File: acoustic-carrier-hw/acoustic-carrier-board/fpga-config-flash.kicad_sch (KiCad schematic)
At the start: 20 parts, among them IC1 ECP5-BGA256, J16 Conn_01x08_Socket, J6 Conn_01x10_Socket, U4 W25Q128JVS, U9 W25Q128JVS

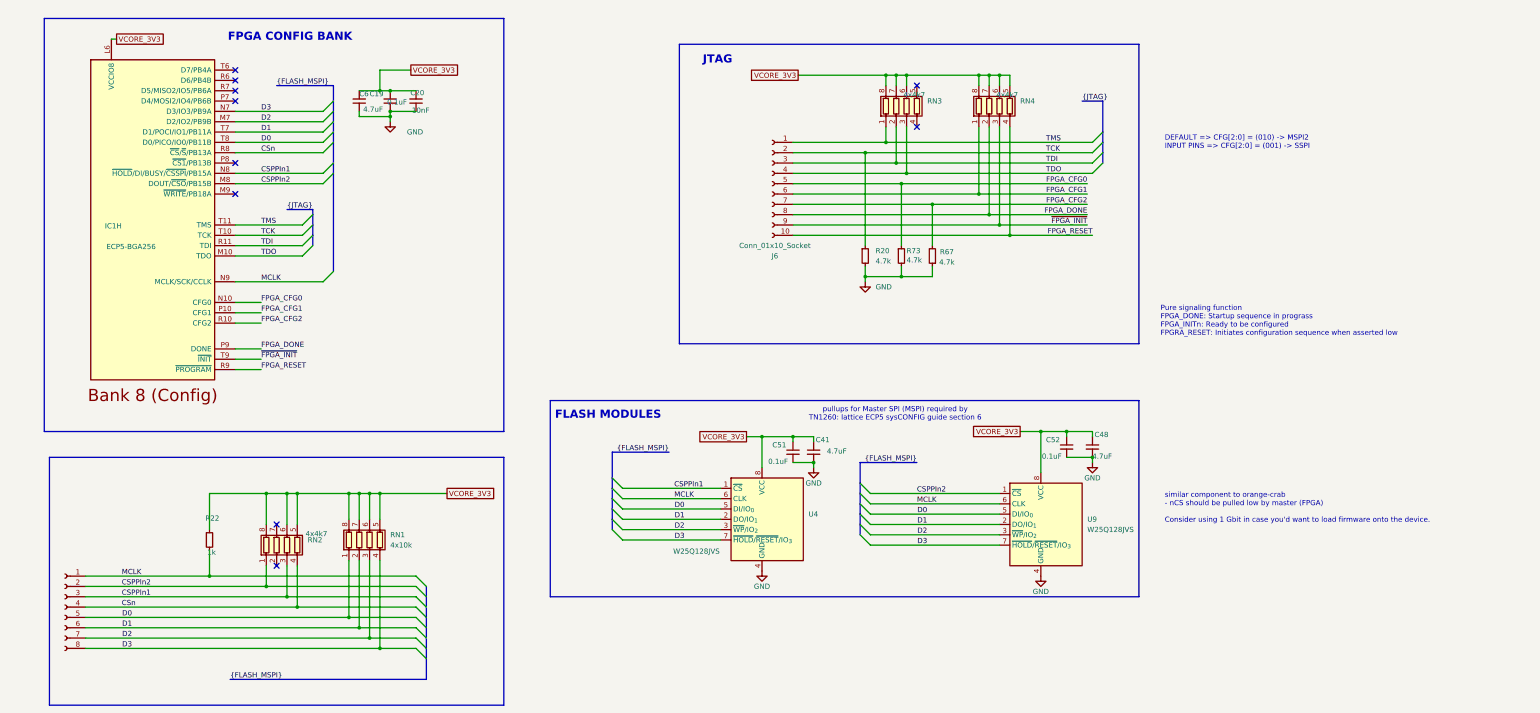
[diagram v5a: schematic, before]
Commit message: [carrier] Added testpoints
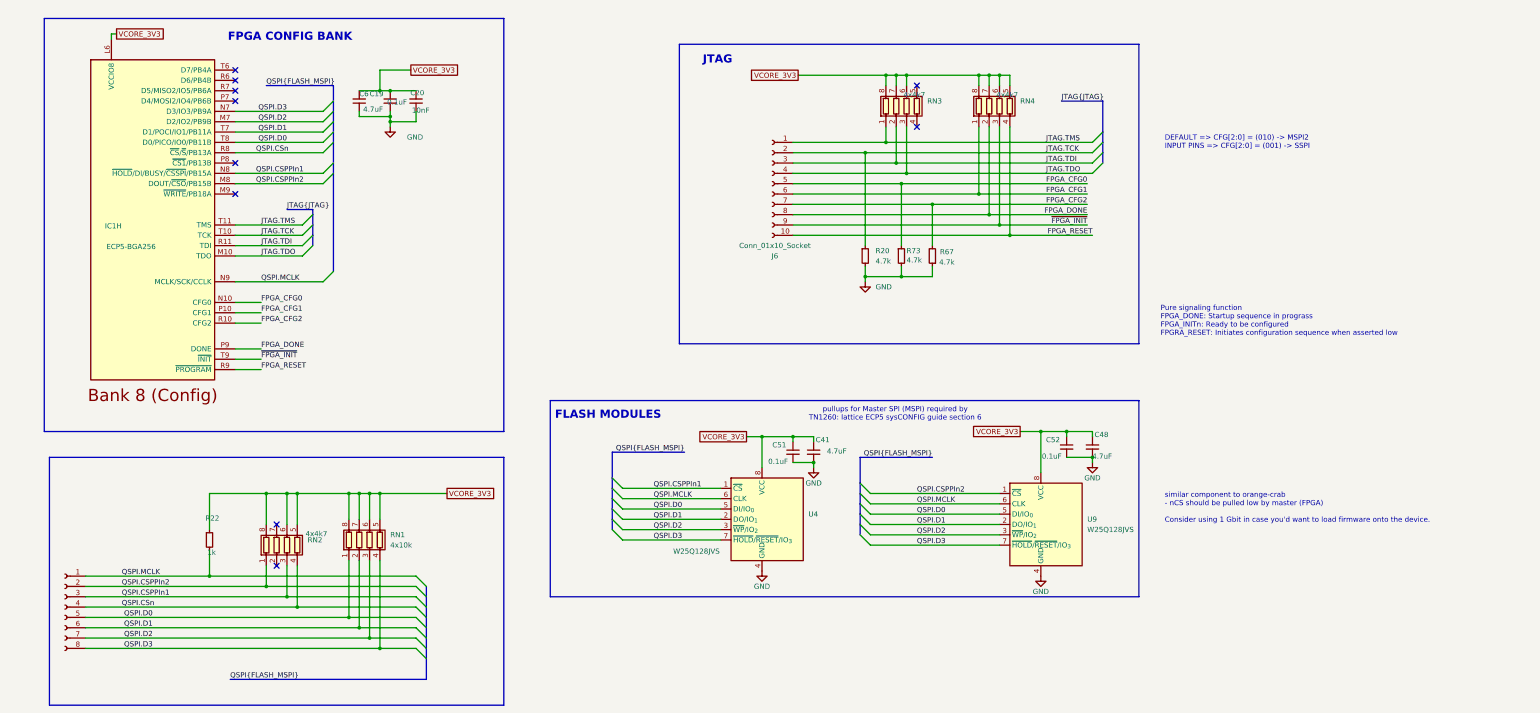
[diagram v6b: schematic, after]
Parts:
- C20: LPN CL05B103KB5NNNC -> C15195; MPN C15195 -> CL05B103KB5NNNC
- R20, R67, R73: LPN 0402WGF4701TCE -> C25900; MPN C25900 -> 0402WGF4701TCE
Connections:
- net CSPPIn1 renamed QSPI.CSPPIn1
- net CSPPIn2 renamed QSPI.CSPPIn2
- net CSn renamed QSPI.CSn
- net D0 renamed QSPI.D0
- net D1 renamed QSPI.D1
- net D2 renamed QSPI.D2
- net D3 renamed QSPI.D3
- net MCLK renamed QSPI.MCLK
- net TCK renamed JTAG.TCK
- net TDI renamed JTAG.TDI
- net TDO renamed JTAG.TDO
- net TMS renamed JTAG.TMS

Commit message: [carrier] Finished rough layout, p (put together according to component category
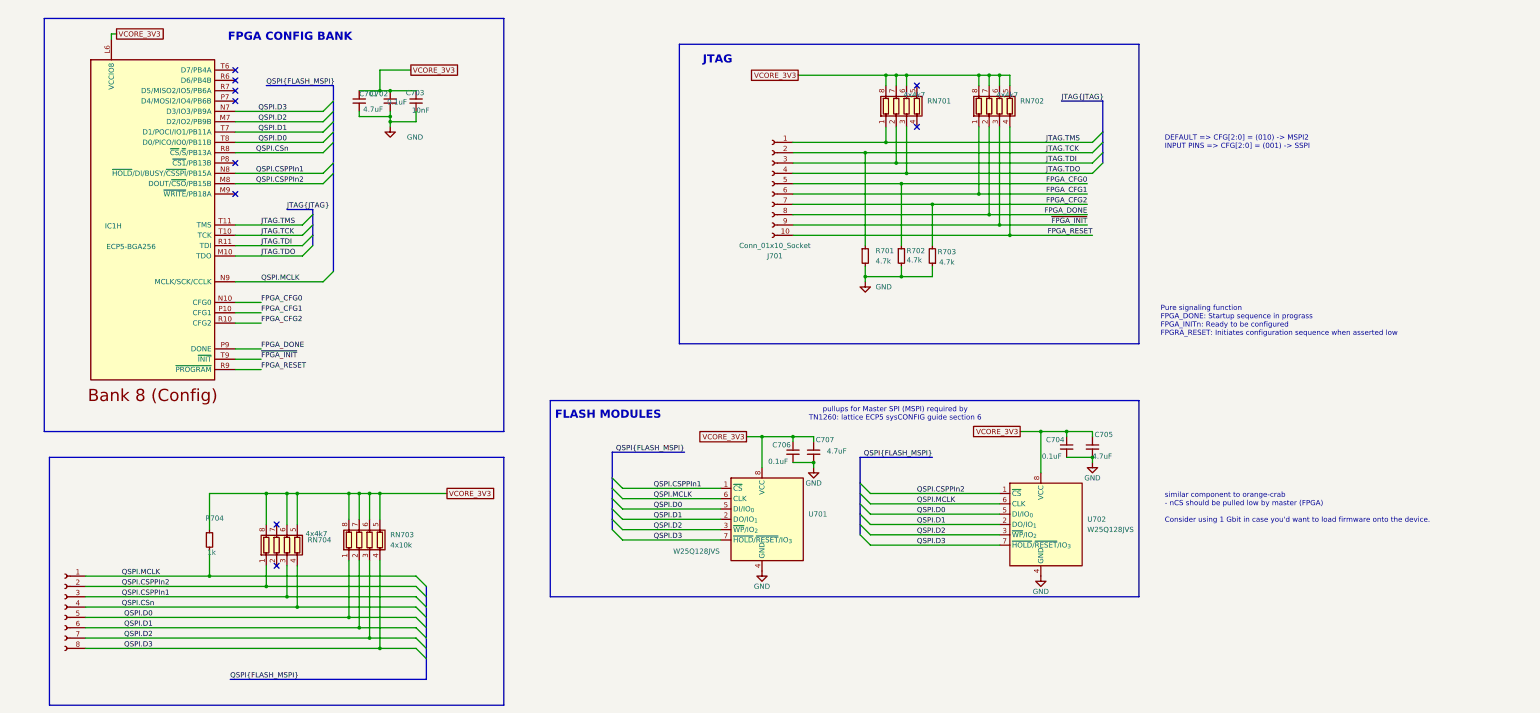
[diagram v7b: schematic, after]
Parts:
- renumbered C6 to C701, C19 to C702, C20 to C703, C52 to C704, C48 to C705, C51 to C706, C41 to C707, J6 to J701, J16 to J702, R20 to R701, R73 to R702, R67 to R703, R22 to R704, RN3 to RN701, RN4 to RN702, RN1 to RN703, RN2 to RN704, U4 to U701, U9 to U702
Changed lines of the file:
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@@
 		(on_board yes)
 		(dnp no)
-		(property "Reference" "#PWR051"
+		(property "Reference" "#PWR0703"
 			(at 271.78 132.08 0)
 			(effects
@@
 			(project "acoustic-carrier-board"
 				(path "/25b015c9-ab13-4427-b72c-b6f348597100/36da1f88-b4f8-4b81-86e1-fac0fb6202fa"
-					(reference "#PWR051")
+					(reference "#PWR0703")
 					(unit 1)
 				)
@@
 		(on_board yes)
 		(dnp no)
-		(property "Reference" "C20"
+		(property "Reference" "C703"
 			(at 107.442 34.798 0)
 			(effects
@@
 			(project "acoustic-carrier-board"
 				(path "/25b015c9-ab13-4427-b72c-b6f348597100/36da1f88-b4f8-4b81-86e1-fac0fb6202fa"
-					(reference "C20")
+					(reference "C703")
 					(unit 1)
 				)
@@
 		(on_board yes)
 		(dnp no)
-		(property "Reference" "C51"
+		(property "Reference" "C706"
 			(at 193.04 121.412 0)
 			(effects
@@
 			(project "acoustic-carrier-board"
 				(path "/25b015c9-ab13-4427-b72c-b6f348597100/36da1f88-b4f8-4b81-86e1-fac0fb6202fa"
-					(reference "C51")
+					(reference "C706")
 					(unit 1)
 				)
@@
 		(on_board yes)
 		(dnp no)
-		(property "Reference" "C6"
+		(property "Reference" "C701"
 			(at 91.44 35.052 0)
 			(effects
@@
 			(project "acoustic-carrier-board"
 				(path "/25b015c9-ab13-4427-b72c-b6f348597100/36da1f88-b4f8-4b81-86e1-fac0fb6202fa"
-					(reference "C6")
+					(reference "C701")
 					(unit 1)
 				)
@@
 		(on_board yes)
 		(dnp no)
-		(property "Reference" "J6"
+		(property "Reference" "J701"
 			(at 193.675 74.93 0)
 			(effects
@@
 			(project "acoustic-carrier-board"
 				(path "/25b015c9-ab13-4427-b72c-b6f348597100/36da1f88-b4f8-4b81-86e1-fac0fb6202fa"
-					(reference "J6")
+					(reference "J701")
 					(unit 1)
 				)
@@
 		(on_board yes)
 		(dnp no)
-		(property "Reference" "R67"
+		(property "Reference" "R703"
 			(at 235.966 73.914 0)
 			(effects
@@
 			(project "acoustic-carrier-board"
 				(path "/25b015c9-ab13-4427-b72c-b6f348597100/36da1f88-b4f8-4b81-86e1-fac0fb6202fa"
-					(reference "R67")
+					(reference "R703")
 					(unit 1)
 				)
@@
 		(on_board yes)
 		(dnp no)
-		(property "Reference" "C41"
+		(property "Reference" "C707"
 			(at 203.708 120.142 0)
 			(effects
@@
 			(project "acoustic-carrier-board"
 				(path "/25b015c9-ab13-4427-b72c-b6f348597100/36da1f88-b4f8-4b81-86e1-fac0fb6202fa"
-					(reference "C41")
+					(reference "C707")
 					(unit 1)
 				)
@@
 		(on_board yes)
 		(dnp no)
-		(property "Reference" "#PWR047"
+		(property "Reference" "#PWR0704"
 			(at 203.2 133.35 0)
 			(effects
@@
 			(project "acoustic-carrier-board"
 				(path "/25b015c9-ab13-4427-b72c-b6f348597100/36da1f88-b4f8-4b81-86e1-fac0fb6202fa"
-					(reference "#PWR047")
+					(reference "#PWR0704")
 					(unit 1)
 				)
@@
 		(on_board yes)
 		(dnp no)
-		(property "Reference" "C48"
+		(property "Reference" "C705"
 			(at 272.288 118.872 0)
 			(effects
@@
 			(project "acoustic-carrier-board"
 				(path "/25b015c9-ab13-4427-b72c-b6f348597100/36da1f88-b4f8-4b81-86e1-fac0fb6202fa"
-					(reference "C48")
+					(reference "C705")
 					(unit 1)
 				)
@@
 		(on_board yes)
 		(dnp no)
-		(property "Reference" "R22"
+		(property "Reference" "R704"
 			(at 53.594 139.446 0)
 			(effects
@@
 			(project "acoustic-carrier-board"
 				(path "/25b015c9-ab13-4427-b72c-b6f348597100/36da1f88-b4f8-4b81-86e1-fac0fb6202fa"
-					(reference "R22")
+					(reference "R704")
 					(unit 1)
 				)
@@
 		(dnp no)
 		(fields_autoplaced yes)
-		(property "Reference" "U9"
+		(property "Reference" "U702"
 			(at 270.51 139.6999 0)
 			(effects
@@
 			(project "acoustic-carrier-board"
 				(path "/25b015c9-ab13-4427-b72c-b6f348597100/36da1f88-b4f8-4b81-86e1-fac0fb6202fa"
-					(reference "U9")
+					(reference "U702")
 					(unit 1)
 				)
@@
 		(dnp no)
 		(fields_autoplaced yes)
-		(property "Reference" "RN1"
+		(property "Reference" "RN703"
 			(at 99.06 143.5099 0)
 			(effects
@@
 			(project "acoustic-carrier-board"
 				(path "/25b015c9-ab13-4427-b72c-b6f348597100/36da1f88-b4f8-4b81-86e1-fac0fb6202fa"
-					(reference "RN1")
+					(reference "RN703")
 					(unit 1)
 				)
@@
 		(on_board yes)
 		(dnp no)
-		(property "Reference" "J16"
+		(property "Reference" "J702"
 			(at 19.685 176.53 0)
 			(effects
@@
 			(project "acoustic-carrier-board"
 				(path "/25b015c9-ab13-4427-b72c-b6f348597100/36da1f88-b4f8-4b81-86e1-fac0fb6202fa"
-					(reference "J16")
+					(reference "J702")
 					(unit 1)
 				)
@@
 		(on_board yes)
 		(dnp no)
-		(property "Reference" "#PWR043"
+		(property "Reference" "#PWR0706"
 			(at 259.08 160.02 0)
 			(effects
@@
 			(project "acoustic-carrier-board"
 				(path "/25b015c9-ab13-4427-b72c-b6f348597100/36da1f88-b4f8-4b81-86e1-fac0fb6202fa"
-					(reference "#PWR043")
+					(reference "#PWR0706")
 					(unit 1)
 				)
@@
 		(on_board yes)
 		(dnp no)
-		(property "Reference" "#PWR039"
+		(property "Reference" "#PWR0705"
 			(at 190.5 158.75 0)
 			(effects
@@
 			(project "acoustic-carrier-board"
 				(path "/25b015c9-ab13-4427-b72c-b6f348597100/36da1f88-b4f8-4b81-86e1-fac0fb6202fa"
-					(reference "#PWR039")
+					(reference "#PWR0705")
 					(unit 1)
 				)
@@
 		(dnp no)
 		(fields_autoplaced yes)
-		(property "Reference" "R20"
+		(property "Reference" "R701"
 			(at 218.44 73.6599 0)
 			(effects
@@
 			(project "acoustic-carrier-board"
 				(path "/25b015c9-ab13-4427-b72c-b6f348597100/36da1f88-b4f8-4b81-86e1-fac0fb6202fa"
-					(reference "R20")
+					(reference "R701")
 					(unit 1)
 				)
@@
 		(on_board yes)
 		(dnp no)
-		(property "Reference" "U4"
+		(property "Reference" "U701"
 			(at 201.93 138.4299 0)
 			(effects
@@
 			(project "acoustic-carrier-board"
 				(path "/25b015c9-ab13-4427-b72c-b6f348597100/36da1f88-b4f8-4b81-86e1-fac0fb6202fa"
-					(reference "U4")
+					(reference "U701")
 					(unit 1)
 				)
@@
 		(dnp no)
 		(fields_autoplaced yes)
-		(property "Reference" "#PWR036"
+		(property "Reference" "#PWR0702"
 			(at 215.9 87.63 0)
 			(effects
@@
 			(project "acoustic-carrier-board"
 				(path "/25b015c9-ab13-4427-b72c-b6f348597100/36da1f88-b4f8-4b81-86e1-fac0fb6202fa"
-					(reference "#PWR036")
+					(reference "#PWR0702")
 					(unit 1)
 				)
@@
 		(on_board yes)
 		(dnp no)
-		(property "Reference" "R73"
+		(property "Reference" "R702"
 			(at 226.06 73.66 0)
 			(effects
@@
 			(project "acoustic-carrier-board"
 				(path "/25b015c9-ab13-4427-b72c-b6f348597100/36da1f88-b4f8-4b81-86e1-fac0fb6202fa"
-					(reference "R73")
+					(reference "R702")
 					(unit 1)
 				)
@@
 		(on_board yes)
 		(dnp no)
-		(property "Reference" "#PWR032"
+		(property "Reference" "#PWR0701"
 			(at 99.06 49.53 0)
 			(effects
@@
 			(project "acoustic-carrier-board"
 				(path "/25b015c9-ab13-4427-b72c-b6f348597100/36da1f88-b4f8-4b81-86e1-fac0fb6202fa"
-					(reference "#PWR032")
+					(reference "#PWR0701")
 					(unit 1)
 				)
@@
 		(on_board yes)
 		(dnp no)
-		(property "Reference" "RN4"
+		(property "Reference" "RN702"
 			(at 254 36.8299 0)
 			(effects
@@
 			(project "acoustic-carrier-board"
 				(path "/25b015c9-ab13-4427-b72c-b6f348597100/36da1f88-b4f8-4b81-86e1-fac0fb6202fa"
-					(reference "RN4")
+					(reference "RN702")
 					(unit 1)
 				)
@@
 		(on_board yes)
 		(dnp no)
-		(property "Reference" "C19"
+		(property "Reference" "C702"
 			(at 93.98 35.052 0)
 			(effects
@@
 			(project "acoustic-carrier-board"
 				(path "/25b015c9-ab13-4427-b72c-b6f348597100/36da1f88-b4f8-4b81-86e1-fac0fb6202fa"
-					(reference "C19")
+					(reference "C702")
 					(unit 1)
 				)
@@
 		(on_board yes)
 		(dnp no)
-		(property "Reference" "RN2"
+		(property "Reference" "RN704"
 			(at 78.74 144.7799 0)
 			(effects
@@
 			(project "acoustic-carrier-board"
 				(path "/25b015c9-ab13-4427-b72c-b6f348597100/36da1f88-b4f8-4b81-86e1-fac0fb6202fa"
-					(reference "RN2")
+					(reference "RN704")
 					(unit 1)
 				)
@@
 		(on_board yes)
 		(dnp no)
-		(property "Reference" "RN3"
+		(property "Reference" "RN701"
 			(at 231.14 36.8299 0)
 			(effects
@@
 			(project "acoustic-carrier-board"
 				(path "/25b015c9-ab13-4427-b72c-b6f348597100/36da1f88-b4f8-4b81-86e1-fac0fb6202fa"
-					(reference "RN3")
+					(reference "RN701")
 					(unit 1)
 				)
@@
 		(on_board yes)
 		(dnp no)
-		(property "Reference" "C52"
+		(property "Reference" "C704"
 			(at 260.35 120.142 0)
 			(effects
@@
 			(project "acoustic-carrier-board"
 				(path "/25b015c9-ab13-4427-b72c-b6f348597100/36da1f88-b4f8-4b81-86e1-fac0fb6202fa"
-					(reference "C52")
+					(reference "C704")
 					(unit 1)
 				)

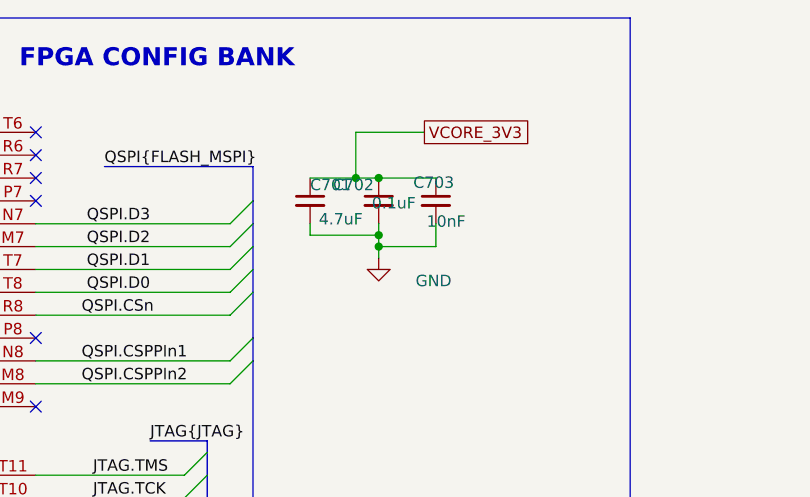
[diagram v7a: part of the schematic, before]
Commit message: [carrier] Removed USB-switch, placed decouplpling for DDR3 and ECP5U (next) consider adding buffers on CC1 and CC2 pins
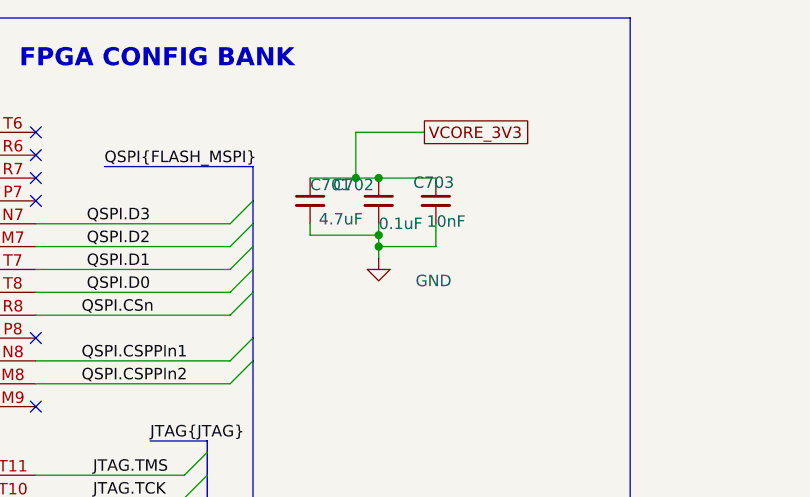
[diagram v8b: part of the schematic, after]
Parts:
- C702, C704, C706: footprint Capacitor_SMD:C_0402_1005Metric -> Capacitor_SMD:C_0201_0603Metric; LPN C307331 -> C22435929; MPN CL05B104KB54PNC -> CGA0201X7R104K160ET
- C703: footprint Capacitor_SMD:C_0402_1005Metric -> Capacitor_SMD:C_0201_0603Metric; LPN C15195 -> C285010; MPN CL05B103KB5NNNC -> 0201B103K250NT
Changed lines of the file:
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@@
 			)
 		)
-		(property "Footprint" "Capacitor_SMD:C_0402_1005Metric"
+		(property "Footprint" "Capacitor_SMD:C_0201_0603Metric"
 			(at 105.41 36.83 0)
 			(effects
@@
 			)
 		)
-		(property "Datasheet" "https://jlcpcb.com/api/file/downloadByFileSystemAccessId/8579707307011465216"
+		(property "Datasheet" "https://jlcpcb.com/api/file/downloadByFileSystemAccessId/8589040499521306624"
 			(at 105.41 36.83 0)
 			(effects
@@
 			)
 		)
-		(property "LPN" "C15195"
+		(property "LPN" "C285010"
 			(at 105.41 36.83 0)
 			(effects
@@
 			)
 		)
-		(property "MPN" "CL05B103KB5NNNC"
+		(property "MPN" "0201B103K250NT"
 			(at 105.41 36.83 0)
 			(effects
@@
 			)
 		)
-		(property "Footprint" "Capacitor_SMD:C_0402_1005Metric"
+		(property "Footprint" "Capacitor_SMD:C_0201_0603Metric"
 			(at 198.12 123.19 0)
 			(effects
@@
 			)
 		)
-		(property "Datasheet" "~"
+		(property "Datasheet" "https://jlcpcb.com/api/file/downloadByFileSystemAccessId/8603345729432014848"
 			(at 198.12 123.19 0)
 			(effects
@@
 			)
 		)
-		(property "LPN" "C307331"
+		(property "LPN" "C22435929"
 			(at 198.12 123.19 0)
 			(effects
@@
 			)
 		)
-		(property "MPN" "CL05B104KB54PNC"
+		(property "MPN" "CGA0201X7R104K160ET "
 			(at 198.12 123.19 0)
 			(effects
@@
 		)
 		(property "Value" "0.1uF"
-			(at 98.298 37.084 0)
+			(at 99.06 39.37 0)
 			(effects
 				(font
@@
 			)
 		)
-		(property "Footprint" "Capacitor_SMD:C_0402_1005Metric"
+		(property "Footprint" "Capacitor_SMD:C_0201_0603Metric"
 			(at 99.06 36.83 0)
 			(effects
@@
 			)
 		)
-		(property "Datasheet" "~"
+		(property "Datasheet" "https://jlcpcb.com/api/file/downloadByFileSystemAccessId/8603345729432014848"
 			(at 99.06 36.83 0)
 			(effects
@@
 			)
 		)
-		(property "LPN" "C307331"
+		(property "LPN" "C22435929"
 			(at 99.06 36.83 0)
 			(effects
@@
 			)
 		)
-		(property "MPN" "CL05B104KB54PNC"
+		(property "MPN" "CGA0201X7R104K160ET "
 			(at 99.06 36.83 0)
 			(effects
@@
 			)
 		)
-		(property "Footprint" "Capacitor_SMD:C_0402_1005Metric"
+		(property "Footprint" "Capacitor_SMD:C_0201_0603Metric"
 			(at 265.43 121.92 0)
 			(effects
@@
 			)
 		)
-		(property "Datasheet" "~"
+		(property "Datasheet" "https://jlcpcb.com/api/file/downloadByFileSystemAccessId/8603345729432014848"
 			(at 265.43 121.92 0)
 			(effects
@@
 			)
 		)
-		(property "LPN" "C307331"
+		(property "LPN" "C22435929"
 			(at 265.43 121.92 0)
 			(effects
@@
 			)
 		)
-		(property "MPN" "CL05B104KB54PNC"
+		(property "MPN" "CGA0201X7R104K160ET "
 			(at 265.43 121.92 0)
 			(effects
